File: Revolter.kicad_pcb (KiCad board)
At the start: 4 copper layers, 93 parts, among them IC1 LM5017, IC2 AP65111, IC3 IRSM005, IC4 IRSM005, IC5 IRSM005, J2 USB_A, P3 IN+, P4 IN-, P5 MOTOR3, P6 MOTOR2, P7 MOTOR1, P8 SWD, U1 STM32F405RGTx, U2 ACS730xLCTR-50AB, U3 ACS730xLCTR-50AB, U4 ACS730xLCTR-50AB, Y1 8MHz

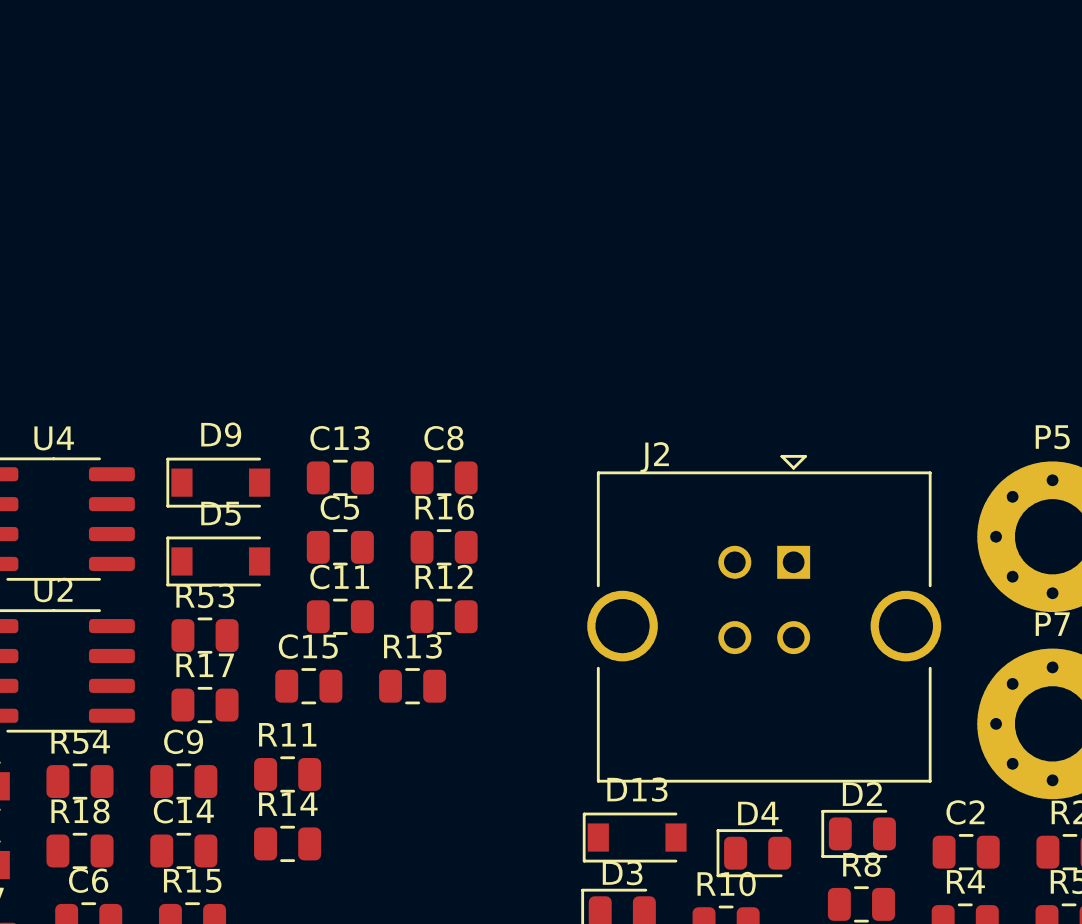
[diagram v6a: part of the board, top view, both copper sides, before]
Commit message: - added temp sensors and fan/pump outputs - made footprint selection
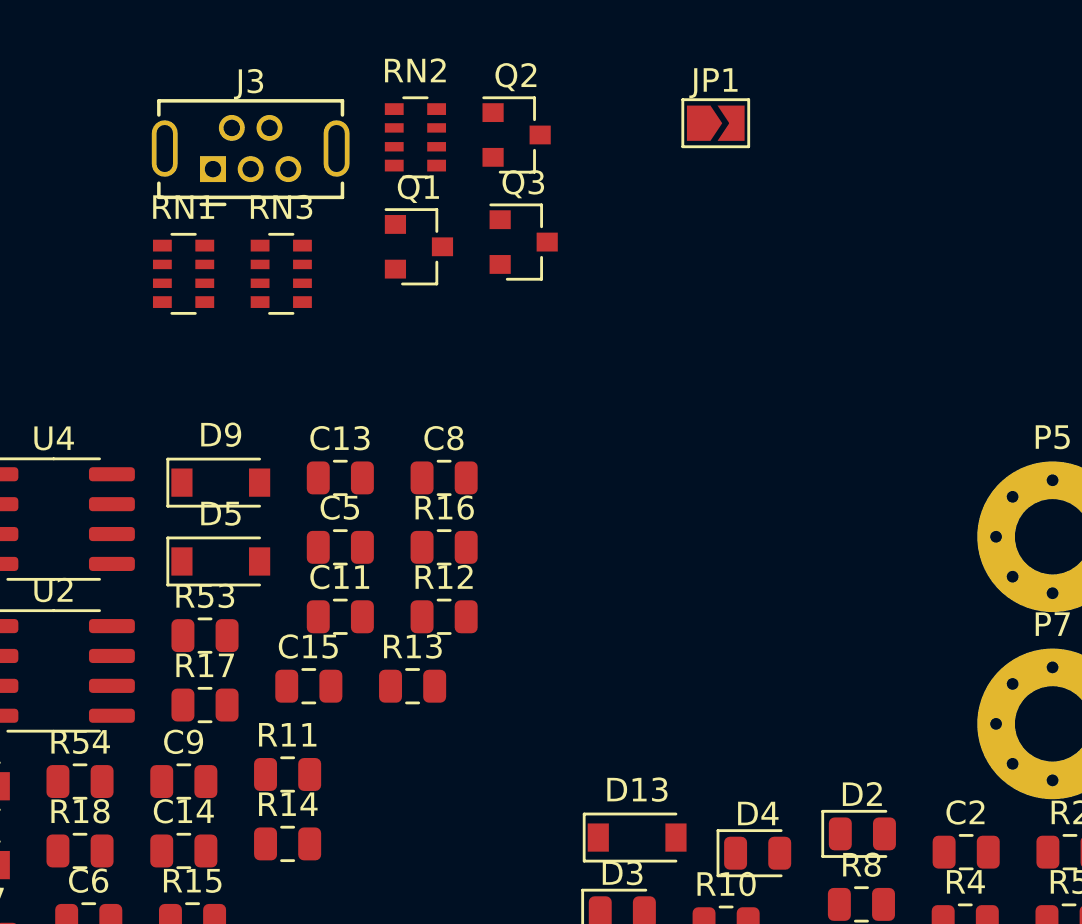
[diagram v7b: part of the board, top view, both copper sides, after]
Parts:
- removed J2: USB_A, Connector_USB:USB_B_TE_5787834_Vertical
- added J3: USB_B_Mini, Connector_USB:USB_Mini-B_Tensility_54-00023_Vertical, F.Cu at (113.5, 55.0)
- added JP1: VCC, Jumper:SolderJumper-2_P1.3mm_Open_TrianglePad1.0x1.5mm, F.Cu at (134.9, 53.0)
- added Q1: Q_NMOS_GSD, Package_TO_SOT_SMD:SOT-23, F.Cu at (122.2, 58.3)
- added Q2: Q_NMOS_GSD, Package_TO_SOT_SMD:SOT-23, F.Cu at (126.4, 53.5)
- added Q3: Q_NMOS_GSD, Package_TO_SOT_SMD:SOT-23, F.Cu at (126.7, 58.1)
- added RN1: 10k, Resistor_SMD:R_Array_Convex_4x0603, F.Cu at (112.2, 59.5)
- added RN2: 10k, Resistor_SMD:R_Array_Convex_4x0603, F.Cu at (122.1, 53.6)
- added RN3: 10k, Resistor_SMD:R_Array_Convex_4x0603, F.Cu at (116.4, 59.5)
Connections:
- net /MCU/ADC_TEMP renamed /MCU/TEMP_MOSFET
- net /MCU/AN_IN renamed /MCU/VOLTAGE_DC
- P8 pad 6: Net-(P8-Pad6) -> (no net)
- U1 pad 14: /MCU/VOLTAGE_U -> (no net)
- U1 pad 2: Net-(U1-Pad2) -> (no net)
- U1 pad 20: /MCU/RX_SDA_NSS -> /TEMP1
- U1 pad 21: /MCU/SCK_ADC_EXT -> /TEMP2
- U1 pad 22: /MCU/MISO_ADC_EXT2 -> /TEMP3
- U1 pad 23: /MCU/TX_SCL_MOSI -> (no net)
- U1 pad 25: Net-(U1-Pad25) -> (no net)
- U1 pad 28: Net-(U1-Pad28) -> (no net)
- U1 pad 29: Net-(U1-Pad29) -> /MCU/PWM_FAN1
- U1 pad 3: Net-(U1-Pad3) -> (no net)
- U1 pad 30: Net-(U1-Pad30) -> /MCU/PWM_FAN2
- U1 pad 33: Net-(U1-Pad33) -> (no net)
- U1 pad 4: Net-(U1-Pad4) -> (no net)
- U1 pad 40: Net-(U1-Pad40) -> (no net)
- U1 pad 50: Net-(U1-Pad50) -> (no net)
- U1 pad 51: Net-(U1-Pad51) -> (no net)
- U1 pad 52: Net-(U1-Pad52) -> (no net)
- U1 pad 53: Net-(U1-Pad53) -> (no net)
- U1 pad 54: Net-(U1-Pad54) -> (no net)
- U1 pad 55: Net-(U1-Pad55) -> /MCU/PWM_PUMP
- U1 pad 56: Net-(U1-Pad56) -> (no net)
- U1 pad 57: Net-(U1-Pad57) -> (no net)
- U1 pad 58: Net-(U1-Pad58) -> (no net)
- U1 pad 59: Net-(U1-Pad59) -> (no net)
- U1 pad 61: /MCU/CAN_RX -> (no net)
- U1 pad 62: /MCU/CAN_TX -> (no net)

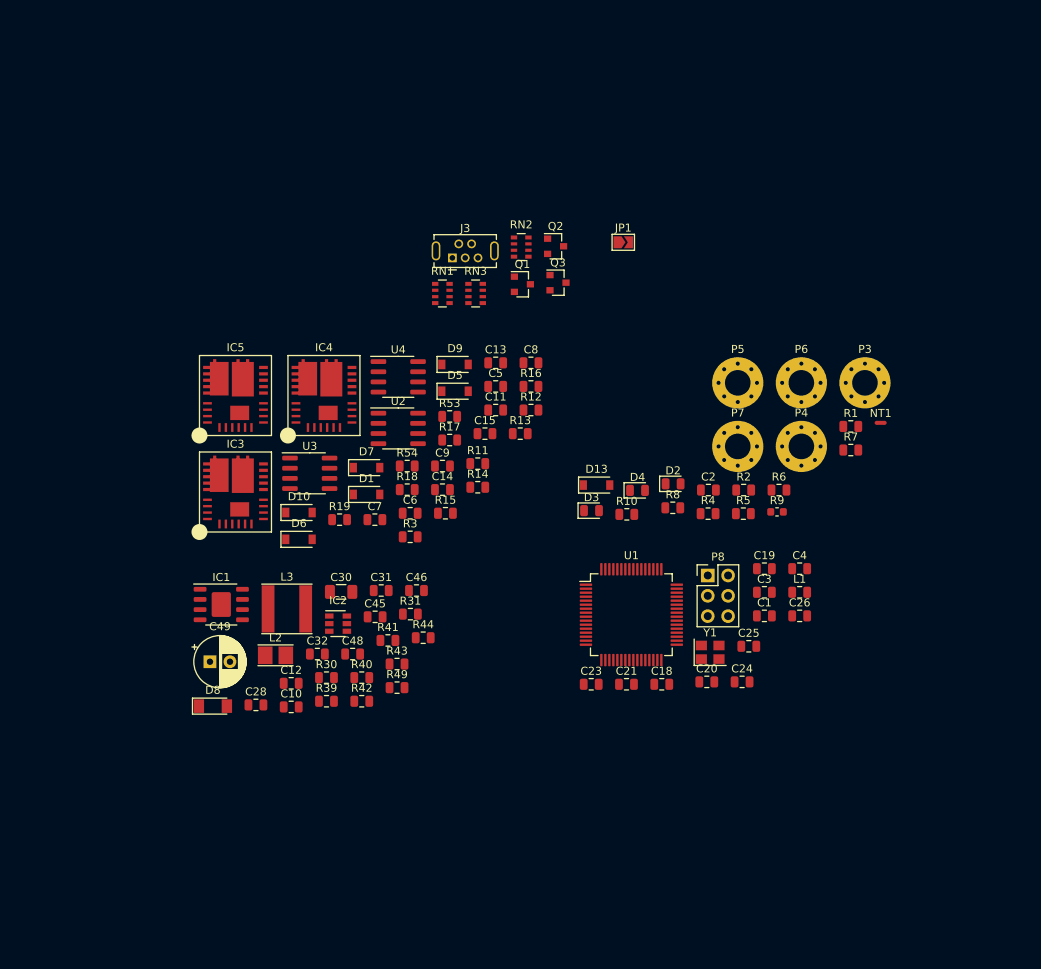
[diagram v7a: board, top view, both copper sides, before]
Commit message: - did most of the layout
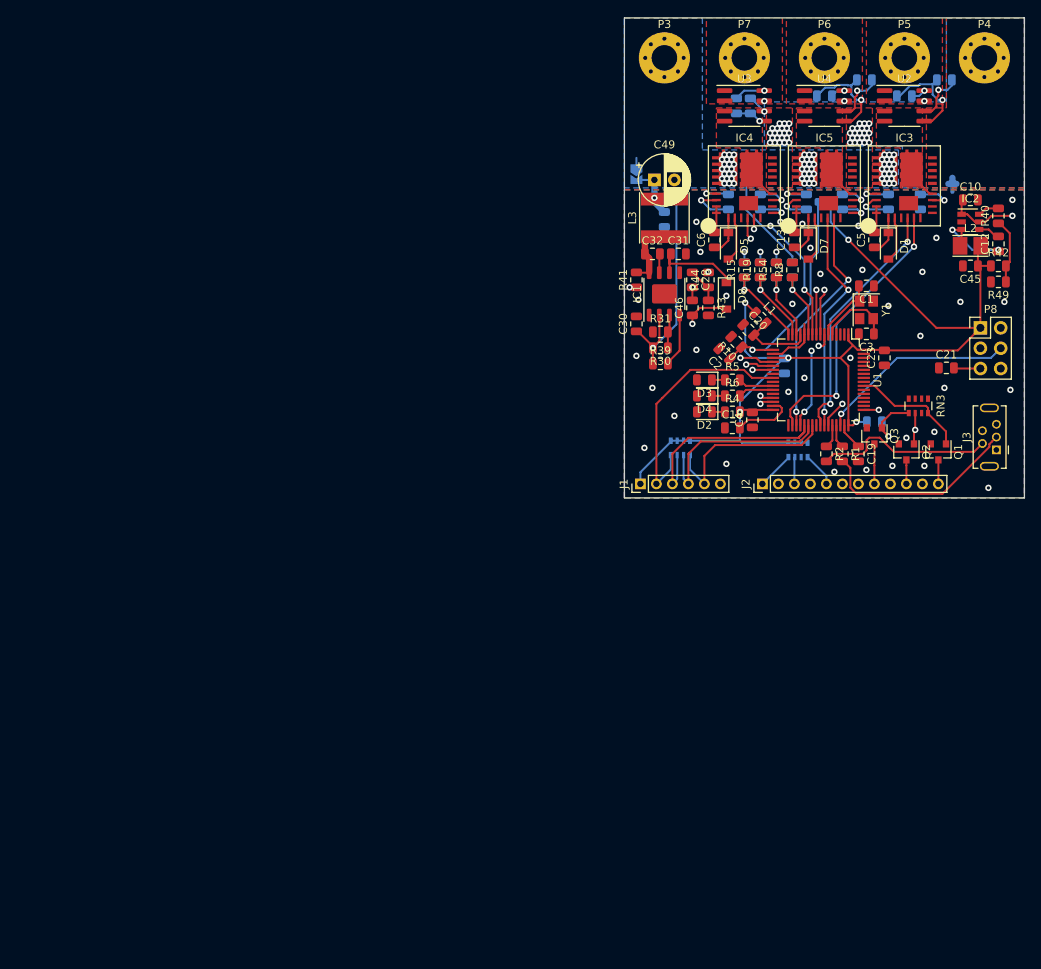
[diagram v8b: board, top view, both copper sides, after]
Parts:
- removed C26: 1u, Capacitor_SMD:C_0805_2012Metric
- removed D10, D13, D6, D9: 3V3, Diode_SMD:D_SOD-123
- added J1: Motor, Connector_PinHeader_2.00mm:PinHeader_1x06_P2.00mm_Vertical, F.Cu at (137.0, 83.2)
- added J2: TEMP, Connector_PinHeader_2.00mm:PinHeader_1x12_P2.00mm_Vertical, F.Cu at (152.2, 83.2)
- C11, C14, C15, C24, C25, C48, C7, C8, C9, JP1, NT1, R11, R12, R13, R14, R16, R17, R18, R3, R53, R7, R9, RN1, RN2: moved to B.Cu
- C30: footprint Capacitor_SMD:C_1206_3216Metric -> Capacitor_SMD:C_0805_2012Metric
- D8: footprint Diode_SMD:D_MiniMELF -> Diode_SMD:D_SOD-123
- R4: value 470R -> 120R
- moved C10 105.9 mm to (178.2, 47.8)
- moved C12 104.1 mm to (181.8, 53.2), turned to 90 degrees
- moved L2 100.8 mm to (178.2, 53.5)
- moved R40 98.3 mm to (181.8, 49.8), turned to 90 degrees
- moved R42 96.4 mm to (181.8, 56.0)
- moved IC2 93.6 mm to (178.2, 50.5)
- moved IC3 92.0 mm to (170.0, 46.0)
- moved R49 90.7 mm to (181.8, 58.0), turned to 180 degrees
- moved C7 89.9 mm to (175.0, 32.8), turned to 180 degrees
- moved C45 86.4 mm to (178.2, 56.0), turned to 180 degrees
- moved D8 82.2 mm to (147.8, 59.8), turned to 270 degrees
- moved C49 81.9 mm to (138.8, 45.2)
- moved IC5 78.1 mm to (160.0, 46.0)
- moved C28 76.2 mm to (143.5, 57.8), turned to 270 degrees
- moved U2 75.0 mm to (170.0, 36.0)
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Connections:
- IC3 pad 28: (no net) -> GND
- IC4 pad 28: (no net) -> GND
- IC5 pad 28: (no net) -> GND
- P5 pad 1: Net-(P5-Pad1) -> /Mosfet driver/Phase_U
- P6 pad 1: Net-(P6-Pad1) -> /Mosfet driver/Phase_V
- P7 pad 1: Net-(P7-Pad1) -> /Mosfet driver/Phase_W
- Q1 pad 3: (no net) -> /PUMP
- Q2 pad 3: (no net) -> /FAN1
- Q3 pad 3: (no net) -> /FAN2
- R53 pad 1: /MCU/VOLTAGE_V -> /MCU/VOLTAGE_U
- R54 pad 1: /MCU/VOLTAGE_V -> /MCU/VOLTAGE_U
- RN1 pad 1: (no net) -> /MCU/HALL_W
- RN1 pad 2: /MCU/HALL_W -> /MCU/HALL_V
- RN1 pad 3: /MCU/HALL_V -> /MCU/HALL_U
- RN1 pad 4: /MCU/HALL_U -> /MCU/TEMP_MOTOR
- RN1 pad 8: (no net) -> +3V3
- RN2 pad 1: /MCU/TEMP_MOTOR -> /TEMP3
- RN2 pad 2: /TEMP3 -> (no net)
- RN3 pad 1: (no net) -> GND
- RN3 pad 7: /MCU/PWM_PUMP -> (no net)
- RN3 pad 8: (no net) -> /MCU/PWM_PUMP
- U1 pad 14: (no net) -> /MCU/VOLTAGE_U
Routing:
- net +3V3: track 0.00 -> 222.8 mm, vias 0 -> 8
- net +12V: track 0.00 -> 152.8 mm, vias 0 -> 4
- net GND: track 0.00 -> 71.5 mm, vias 0 -> 39
- net +BATT: track 0.00 -> 45.7 mm, vias 0 -> 64
- net /MCU/CURRENT_V: track 0.00 -> 36.5 mm, vias 0 -> 2
- net /MCU/LU: track 0.00 -> 34.8 mm, vias 0 -> 2
- net /MCU/CURRENT_U: track 0.00 -> 34.6 mm, vias 0 -> 2
- net /Mosfet driver/Phase_U: track 0.00 -> 33.8 mm, vias 0 -> 1
- net /MCU/CURRENT_W: track 0.00 -> 32.9 mm, vias 0 -> 3
- net /MCU/HW: track 0.00 -> 31.6 mm, vias 0 -> 2
- net /MCU/HU: track 0.00 -> 31.1 mm, vias 0 -> 2
- net /MCU/TEMP_MOTOR: track 0.00 -> 31.1 mm
- net /MCU/LW: track 0.00 -> 29.9 mm, vias 0 -> 3
- net /MCU/LV: track 0.00 -> 29.4 mm, vias 0 -> 2
- net /MCU/TEMP_MOSFET: track 0.00 -> 29.0 mm, vias 0 -> 1
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- added copper zone on B.Cu, net +BATT
- added copper zone on F.Cu, net /Mosfet driver/Phase_U
- added copper zone on F.Cu, net /Mosfet driver/Phase_V
- added copper zone on F.Cu, net /Mosfet driver/Phase_W
- added copper zone on B.Cu, net GND
- added copper zone on F.Cu, net GND
- added copper zone on Sig, net GND
- added copper zone on B.Cu, net GNDPWR
- added copper zone on F.Cu, net GNDPWR
- added copper zone on F.Cu, net Net-(IC3-Pad10)
- added copper zone on F.Cu, net Net-(IC4-Pad10)
- added copper zone on F.Cu, net Net-(IC5-Pad10)
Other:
- board outline added: 50 x 60 mm
